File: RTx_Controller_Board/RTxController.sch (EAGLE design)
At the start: 212 parts, among them IC2 MAX5984C, J22 Debug Header, SW1 COM08720, U1 STM32F407ZXT, U3 KSZ8081, X4 MINI-USB-32005-301, X8 0826-1X1T-GJ-F

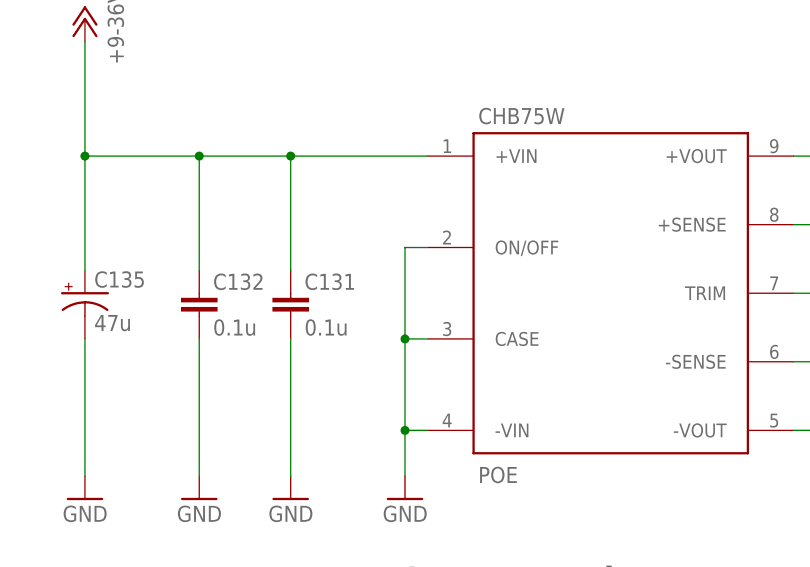
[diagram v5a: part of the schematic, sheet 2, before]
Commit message: PoE power supply ON/OFF connection changed to open circuit, to remain ON.
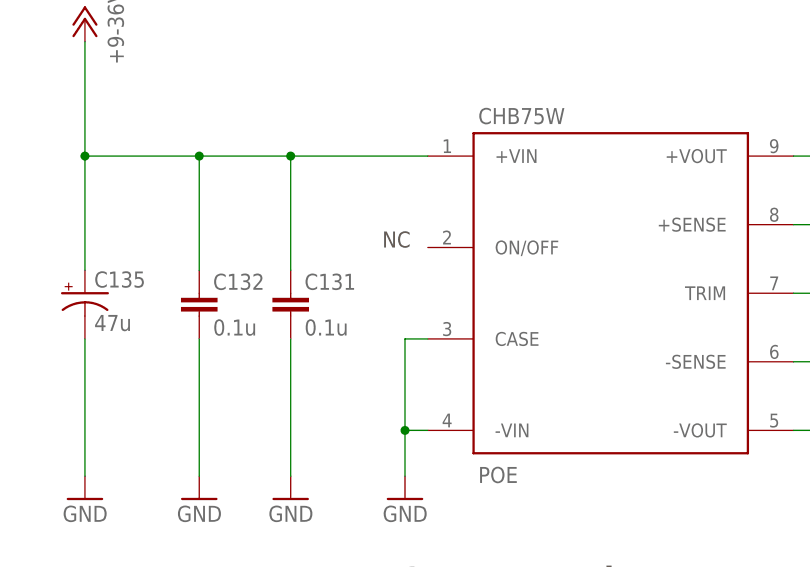
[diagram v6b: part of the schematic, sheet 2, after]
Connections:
- net GND: no longer POE.ON/OFF@2
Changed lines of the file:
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@@
 <wire x1="341.884" y1="244.856" x2="341.884" y2="217.932" width="0.1524" layer="97"/>
 <wire x1="374.904" y1="244.856" x2="374.904" y2="217.932" width="0.1524" layer="97"/>
+<text x="248.92" y="83.82" size="1.778" layer="97">NC</text>
 </plain>
 <instances>
@@
 <pinref part="POE" gate="G$1" pin="-VIN@4"/>
 <wire x1="254" y1="63.5" x2="251.46" y2="63.5" width="0.1524" layer="91"/>
-<pinref part="POE" gate="G$1" pin="ON/OFF@2"/>
-<wire x1="254" y1="83.82" x2="251.46" y2="83.82" width="0.1524" layer="91"/>
 <pinref part="POE" gate="G$1" pin="CASE@3"/>
 <wire x1="251.46" y1="73.66" x2="254" y2="73.66" width="0.1524" layer="91"/>
-<wire x1="251.46" y1="83.82" x2="251.46" y2="73.66" width="0.1524" layer="91"/>
-<junction x="251.46" y="73.66"/>
 <wire x1="251.46" y1="73.66" x2="251.46" y2="63.5" width="0.1524" layer="91"/>
 <junction x="251.46" y="63.5"/>

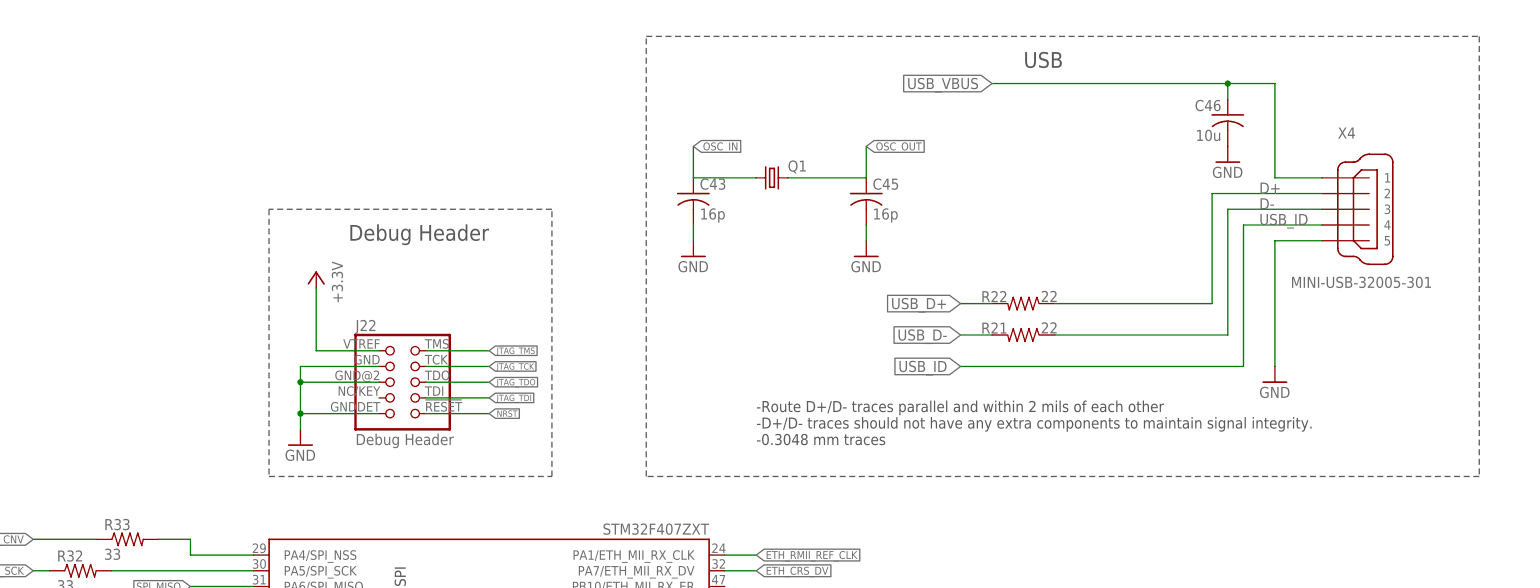
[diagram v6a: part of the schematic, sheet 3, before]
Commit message: Additional RTx Controller layout performed.
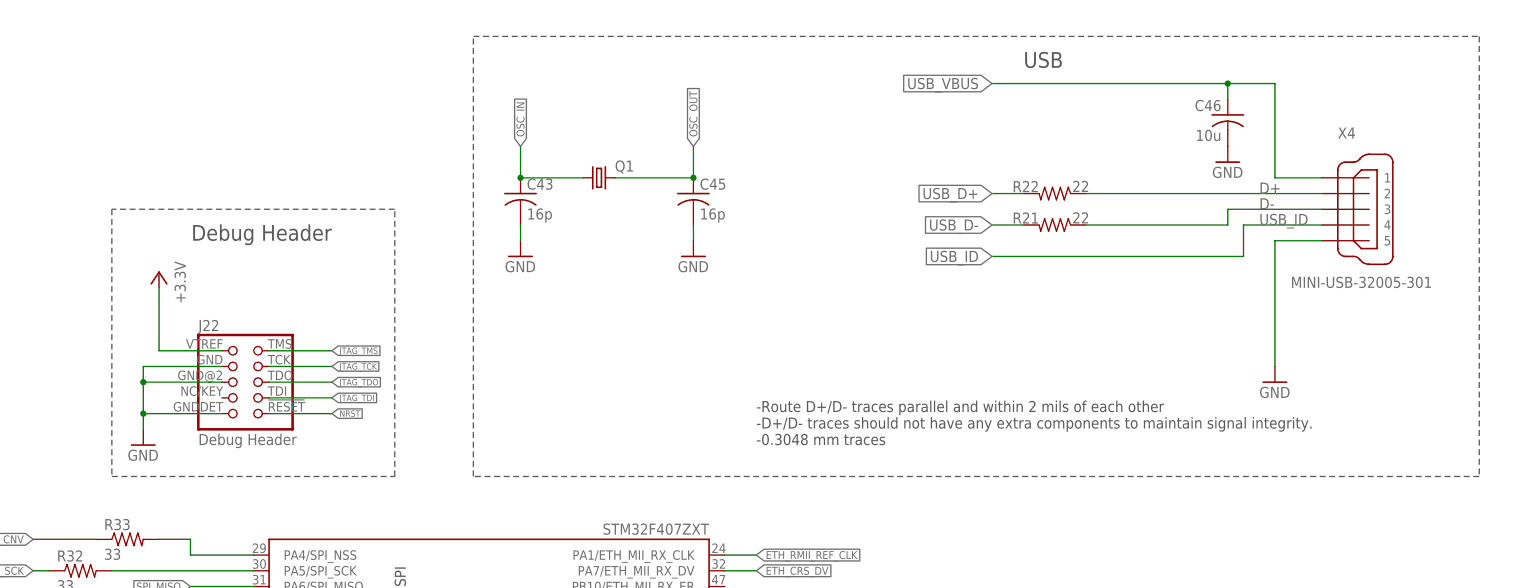
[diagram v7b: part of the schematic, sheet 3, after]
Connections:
- net SPI_MISO: now also U1-IO.PE7@38
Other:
- moved on the sheet: C43, C45, J22, Q1, R21, R22
